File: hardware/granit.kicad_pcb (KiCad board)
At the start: 4 copper layers, 71 x 101 mm, 0 parts

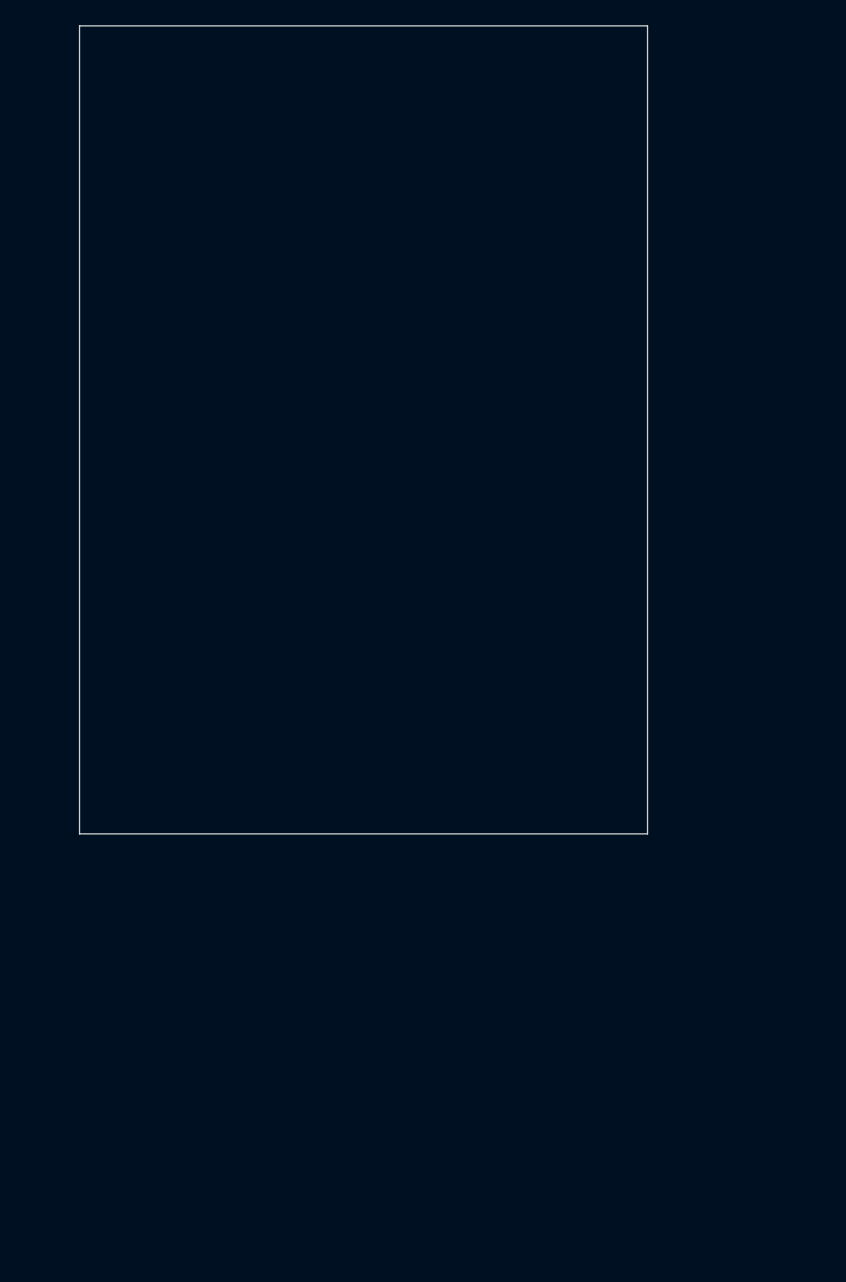
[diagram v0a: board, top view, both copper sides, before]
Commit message: Add 4x M3 mounting holes at board corners (3mm from edges)
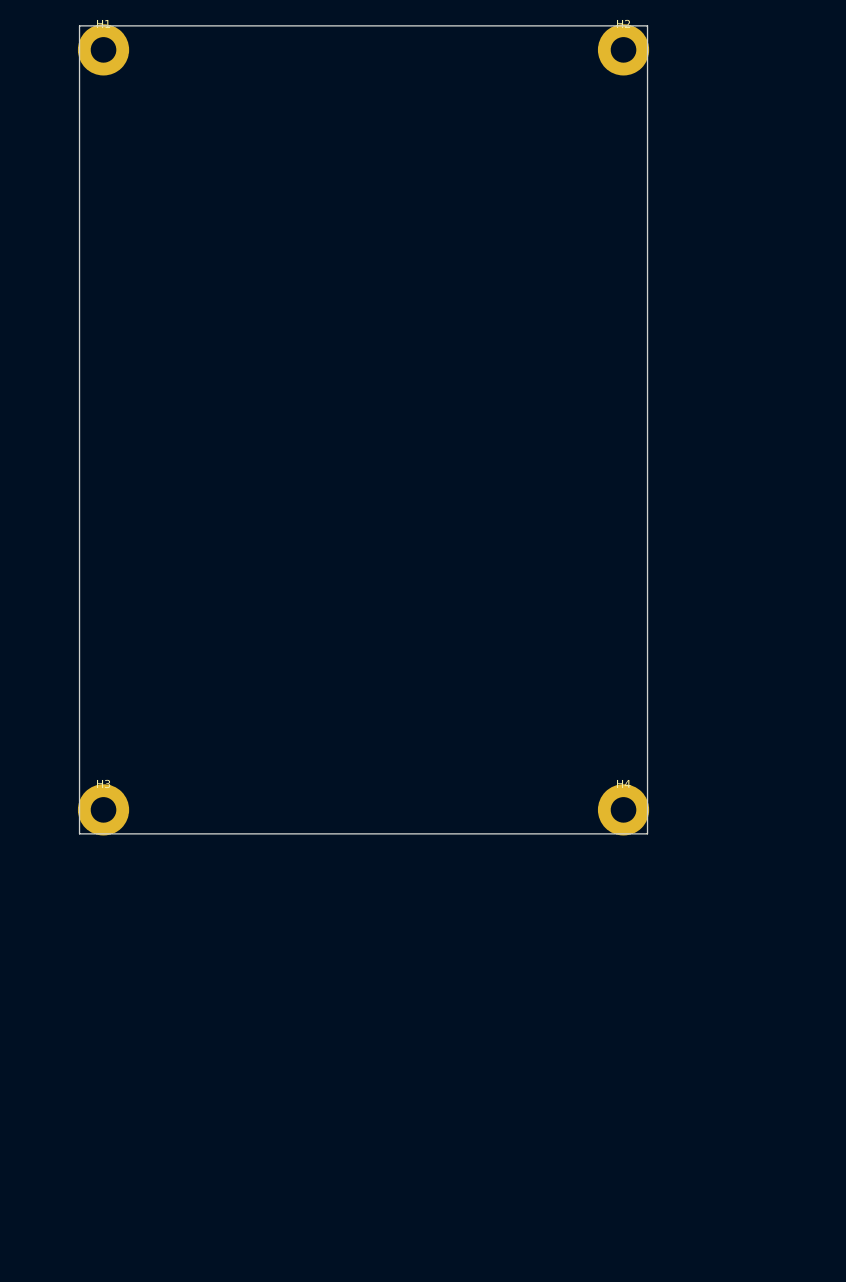
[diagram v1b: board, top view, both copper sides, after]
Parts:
- added H1: MountingHole, MountingHole:MountingHole_3.2mm_M3_Pad_Via, F.Cu at (23.0, 23.0)
- added H2: MountingHole, MountingHole:MountingHole_3.2mm_M3_Pad_Via, F.Cu at (88.0, 23.0)
- added H3: MountingHole, MountingHole:MountingHole_3.2mm_M3_Pad_Via, F.Cu at (23.0, 118.0)
- added H4: MountingHole, MountingHole:MountingHole_3.2mm_M3_Pad_Via, F.Cu at (88.0, 118.0)
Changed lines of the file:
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@@
 	)
 	(embedded_fonts no)
+	(footprint "MountingHole:MountingHole_3.2mm_M3_Pad_Via"
+		(layer "F.Cu")
+		(at 23 23)
+		(property "Reference" "H1"
+			(at 0 -3.2 0)
+			(layer "F.SilkS")
+			(effects
+				(font
+					(size 1 1)
+					(thickness 0.15)
+				)
+			)
+		)
+		(property "Value" "MountingHole"
+			(at 0 3.2 0)
+			(layer "F.Fab")
+			(effects
+				(font
+					(size 1 1)
+					(thickness 0.15)
+				)
+			)
+		)
+		(pad "1" thru_hole circle
+			(at 0 0)
+			(size 6.4 6.4)
+			(drill 3.2)
+			(layers "*.Cu" "*.Mask")
+			(remove_unused_layers no)
+		)
+	)
+	(footprint "MountingHole:MountingHole_3.2mm_M3_Pad_Via"
+		(layer "F.Cu")
+		(at 88 23)
+		(property "Reference" "H2"
+			(at 0 -3.2 0)
+			(layer "F.SilkS")
+			(effects
+				(font
+					(size 1 1)
+					(thickness 0.15)
+				)
+			)
+		)
+		(property "Value" "MountingHole"
+			(at 0 3.2 0)
+			(layer "F.Fab")
+			(effects
+				(font
+					(size 1 1)
+					(thickness 0.15)
+				)
+			)
+		)
+		(pad "1" thru_hole circle
+			(at 0 0)
+			(size 6.4 6.4)
+			(drill 3.2)
+			(layers "*.Cu" "*.Mask")
+			(remove_unused_layers no)
+		)
+	)
+	(footprint "MountingHole:MountingHole_3.2mm_M3_Pad_Via"
+		(layer "F.Cu")
+		(at 23 118)
+		(property "Reference" "H3"
+			(at 0 -3.2 0)
+			(layer "F.SilkS")
+			(effects
+				(font
+					(size 1 1)
+					(thickness 0.15)
+				)
+			)
+		)
+		(property "Value" "MountingHole"
+			(at 0 3.2 0)
+			(layer "F.Fab")
+			(effects
+				(font
+					(size 1 1)
+					(thickness 0.15)
+				)
+			)
+		)
+		(pad "1" thru_hole circle
+			(at 0 0)
+			(size 6.4 6.4)
+			(drill 3.2)
+			(layers "*.Cu" "*.Mask")
+			(remove_unused_layers no)
+		)
+	)
+	(footprint "MountingHole:MountingHole_3.2mm_M3_Pad_Via"
+		(layer "F.Cu")
+		(at 88 118)
+		(property "Reference" "H4"
+			(at 0 -3.2 0)
+			(layer "F.SilkS")
+			(effects
+				(font
+					(size 1 1)
+					(thickness 0.15)
+				)
+			)
+		)
+		(property "Value" "MountingHole"
+			(at 0 3.2 0)
+			(layer "F.Fab")
+			(effects
+				(font
+					(size 1 1)
+					(thickness 0.15)
+				)
+			)
+		)
+		(pad "1" thru_hole circle
+			(at 0 0)
+			(size 6.4 6.4)
+			(drill 3.2)
+			(layers "*.Cu" "*.Mask")
+			(remove_unused_layers no)
+		)
+	)
 )

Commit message: Move mounting holes to 4mm from edges (pad fits inside board)
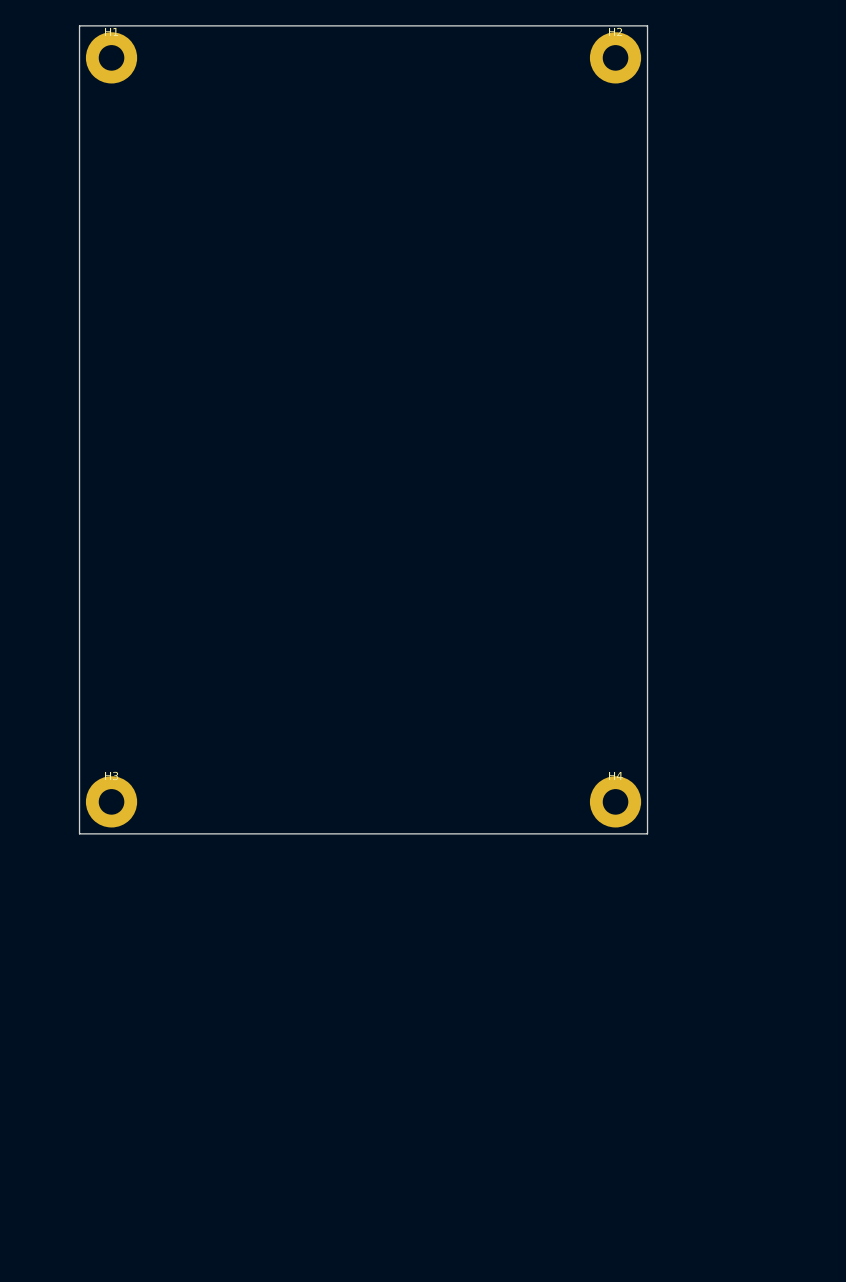
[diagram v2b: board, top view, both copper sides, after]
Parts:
- moved H1 1.41 mm to (24.0, 24.0)
- moved H2 1.41 mm to (87.0, 24.0)
- moved H3 1.41 mm to (24.0, 117.0)
- moved H4 1.41 mm to (87.0, 117.0)
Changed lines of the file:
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@@
 	(footprint "MountingHole:MountingHole_3.2mm_M3_Pad_Via"
 		(layer "F.Cu")
-		(at 23 23)
+		(at 24 24)
 		(property "Reference" "H1"
 			(at 0 -3.2 0)
@@
 	(footprint "MountingHole:MountingHole_3.2mm_M3_Pad_Via"
 		(layer "F.Cu")
-		(at 88 23)
+		(at 87 24)
 		(property "Reference" "H2"
 			(at 0 -3.2 0)
@@
 	(footprint "MountingHole:MountingHole_3.2mm_M3_Pad_Via"
 		(layer "F.Cu")
-		(at 23 118)
+		(at 24 117)
 		(property "Reference" "H3"
 			(at 0 -3.2 0)
@@
 	(footprint "MountingHole:MountingHole_3.2mm_M3_Pad_Via"
 		(layer "F.Cu")
-		(at 88 118)
+		(at 87 117)
 		(property "Reference" "H4"
 			(at 0 -3.2 0)

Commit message: Switch to Hammond 1455T2201 (160mm wide, fits 3.5" HDD)
- PCB: 71 × 155mm (was 71 × 101mm)
- Case: 220 × 160 × 51.5mm
- Updated board outline, mounting holes, README, TODO, assembly
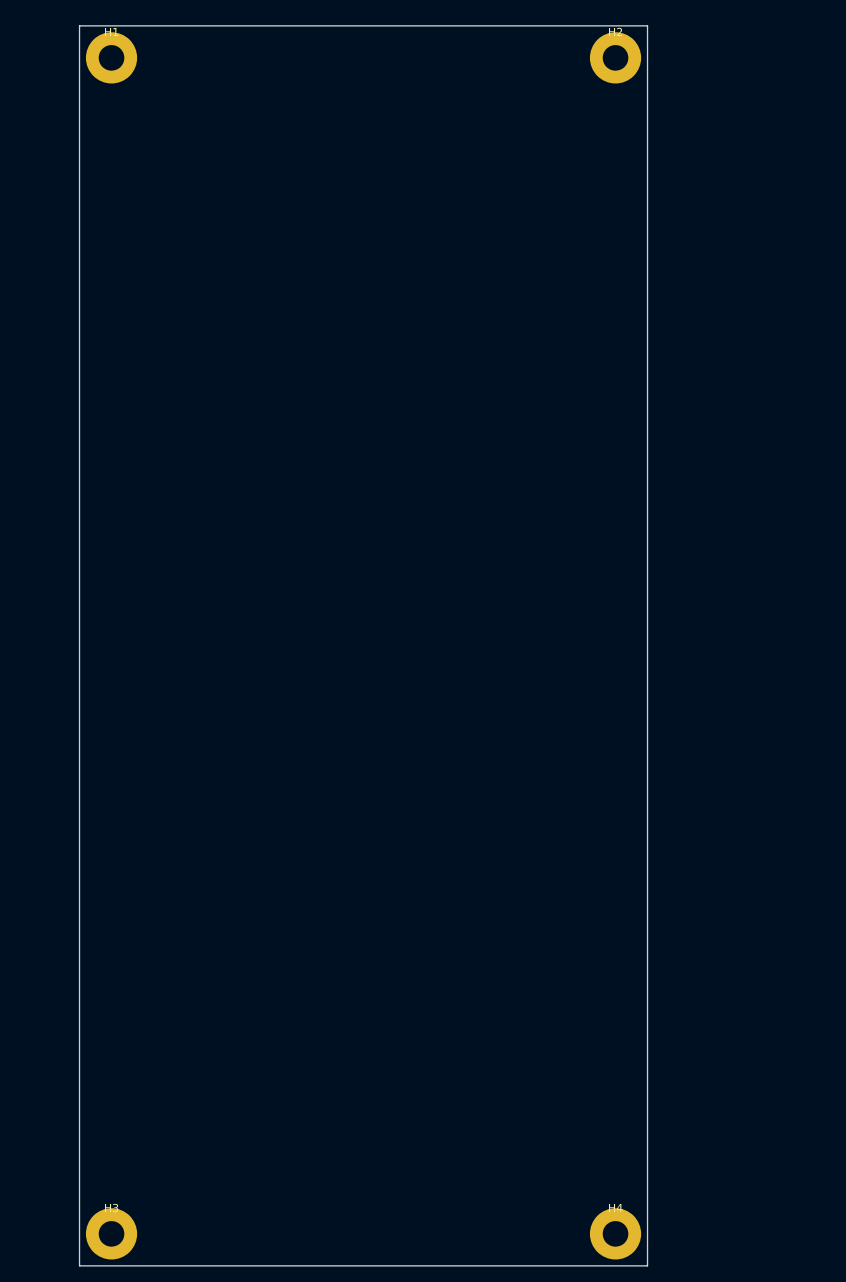
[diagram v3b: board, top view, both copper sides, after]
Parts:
- moved H3 54.0 mm to (24.0, 171.0)
- moved H4 54.0 mm to (87.0, 171.0)
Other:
- board size 71 x 101 mm -> 71 x 155 mm
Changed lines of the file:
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@@
 	(gr_rect
 		(start 20 20)
-		(end 91 121)
+		(end 91 175)
 		(stroke
 			(width 0.1)
@@
 	(footprint "MountingHole:MountingHole_3.2mm_M3_Pad_Via"
 		(layer "F.Cu")
-		(at 24 117)
+		(at 24 171)
 		(property "Reference" "H3"
 			(at 0 -3.2 0)
@@
 	(footprint "MountingHole:MountingHole_3.2mm_M3_Pad_Via"
 		(layer "F.Cu")
-		(at 87 117)
+		(at 87 171)
 		(property "Reference" "H4"
 			(at 0 -3.2 0)

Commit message: Keep PCB at 71x101mm — sized for electronics, reusable with 2.5" or 3.5" HDD
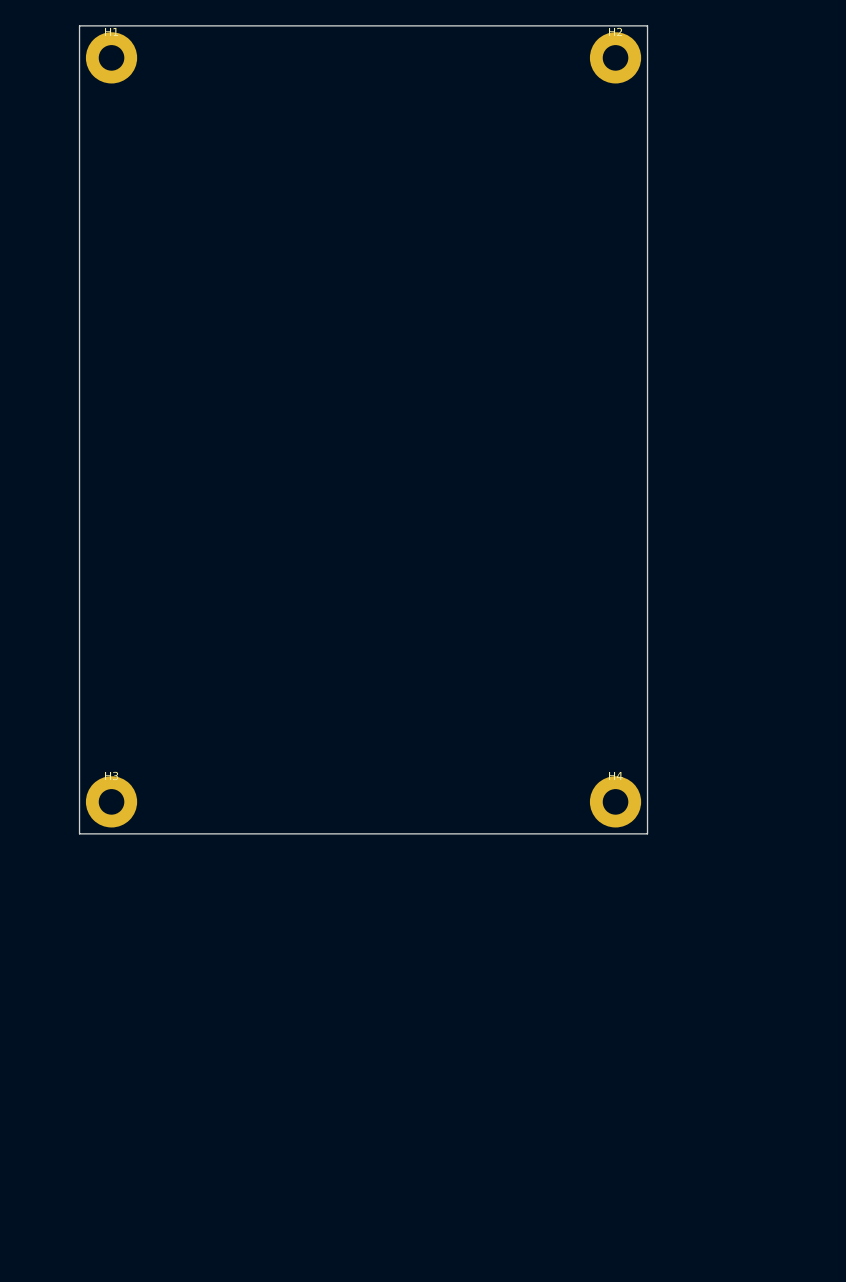
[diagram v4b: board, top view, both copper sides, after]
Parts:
- moved H3 54.0 mm to (24.0, 117.0)
- moved H4 54.0 mm to (87.0, 117.0)
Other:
- board size 71 x 155 mm -> 71 x 101 mm
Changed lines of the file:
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@@
 	(gr_rect
 		(start 20 20)
-		(end 91 175)
+		(end 91 121)
 		(stroke
 			(width 0.1)
@@
 	(footprint "MountingHole:MountingHole_3.2mm_M3_Pad_Via"
 		(layer "F.Cu")
-		(at 24 171)
+		(at 24 117)
 		(property "Reference" "H3"
 			(at 0 -3.2 0)
@@
 	(footprint "MountingHole:MountingHole_3.2mm_M3_Pad_Via"
 		(layer "F.Cu")
-		(at 87 171)
+		(at 87 117)
 		(property "Reference" "H4"
 			(at 0 -3.2 0)

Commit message: PCB 71x99mm — fits both 1455L (slim, 2.5" HDD) and 1455T (wide, 3.5" HDD)
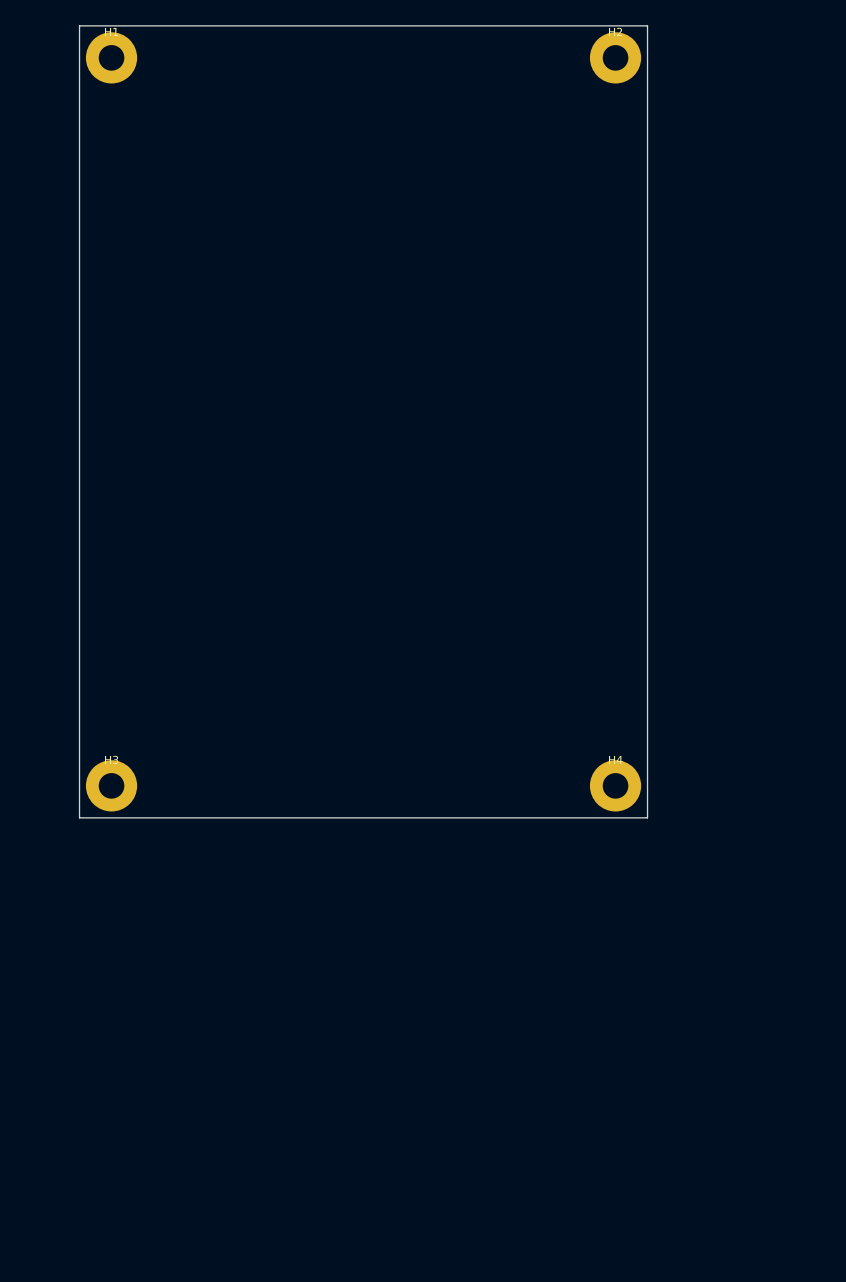
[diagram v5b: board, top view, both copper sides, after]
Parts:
- moved H3 2.00 mm to (24.0, 115.0)
- moved H4 2.00 mm to (87.0, 115.0)
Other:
- board size 71 x 101 mm -> 71 x 99 mm
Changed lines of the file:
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@@
 	(gr_rect
 		(start 20 20)
-		(end 91 121)
+		(end 91 119)
 		(stroke
 			(width 0.1)
@@
 	(footprint "MountingHole:MountingHole_3.2mm_M3_Pad_Via"
 		(layer "F.Cu")
-		(at 24 117)
+		(at 24 115)
 		(property "Reference" "H3"
 			(at 0 -3.2 0)
@@
 	(footprint "MountingHole:MountingHole_3.2mm_M3_Pad_Via"
 		(layer "F.Cu")
-		(at 87 117)
+		(at 87 115)
 		(property "Reference" "H4"
 			(at 0 -3.2 0)

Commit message: PCB layout prep: resize to 92x100mm, fix 3D models, dual assembly variants
- Resize PCB from 71x99mm to 92x100mm for Hammond 1455 enclosures
- Update wide enclosure from 1455T2201 to 1455T2601 (260mm) for 3.5" HDD
- Download CM4 3D model, create AP64501 stand-in, fix KICAD6->KICAD10 paths
- Generate 1455T2601 STEP by scaling T2201
- Create 2.5" HDD placeholder model with SATA recess
- Rewrite assembly script for slim (1455L+2.5") and wide (1455T+3.5") variants
- Render 4K assembly screenshots with software OpenGL
- Update README with new enclosure specs and both assembly images
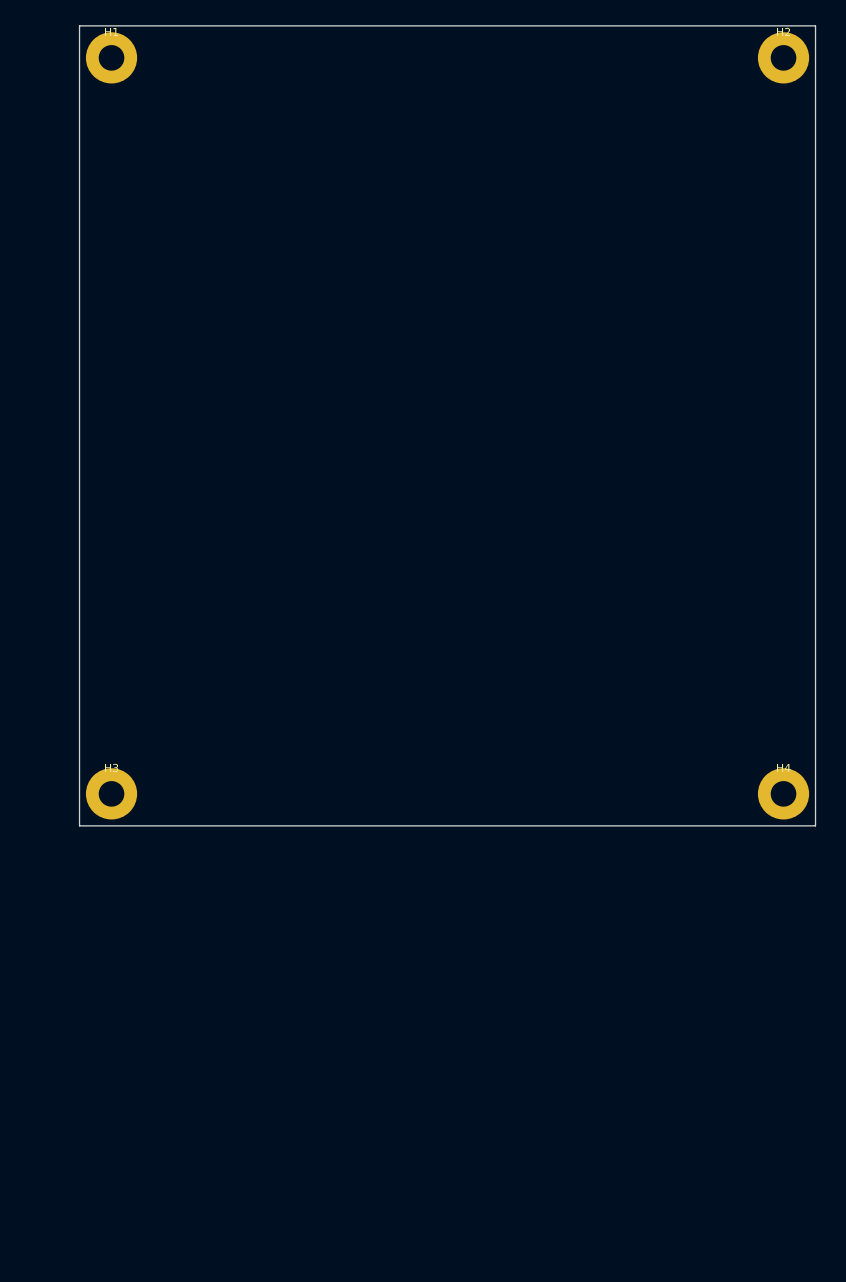
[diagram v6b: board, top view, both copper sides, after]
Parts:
- moved H4 21.0 mm to (108.0, 116.0)
- moved H2 21.0 mm to (108.0, 24.0)
- moved H3 1.00 mm to (24.0, 116.0)
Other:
- board size 71 x 99 mm -> 92 x 100 mm
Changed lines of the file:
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@@
 	(gr_rect
 		(start 20 20)
-		(end 91 119)
+		(end 112 120)
 		(stroke
 			(width 0.1)
@@
 	(footprint "MountingHole:MountingHole_3.2mm_M3_Pad_Via"
 		(layer "F.Cu")
-		(at 87 24)
+		(at 108 24)
 		(property "Reference" "H2"
 			(at 0 -3.2 0)
@@
 	(footprint "MountingHole:MountingHole_3.2mm_M3_Pad_Via"
 		(layer "F.Cu")
-		(at 24 115)
+		(at 24 116)
 		(property "Reference" "H3"
 			(at 0 -3.2 0)
@@
 	(footprint "MountingHole:MountingHole_3.2mm_M3_Pad_Via"
 		(layer "F.Cu")
-		(at 87 115)
+		(at 108 116)
 		(property "Reference" "H4"
 			(at 0 -3.2 0)
